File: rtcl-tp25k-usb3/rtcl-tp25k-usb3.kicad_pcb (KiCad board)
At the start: 4 copper layers, 80 x 35 mm, 82 parts, among them J1 ZX360D-B-10P(30), J10 SSQ-106-02-F-D-RA, J2 0525592253, J3 BTB-DF40C-60DS-0.4V(51), J4 DF40C-60DS-0.4V(51), J5 JTAG, Q1 2SK3018, Q2 2SK3018, U1 FT601Q, U2 TPD4E05U06DQA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

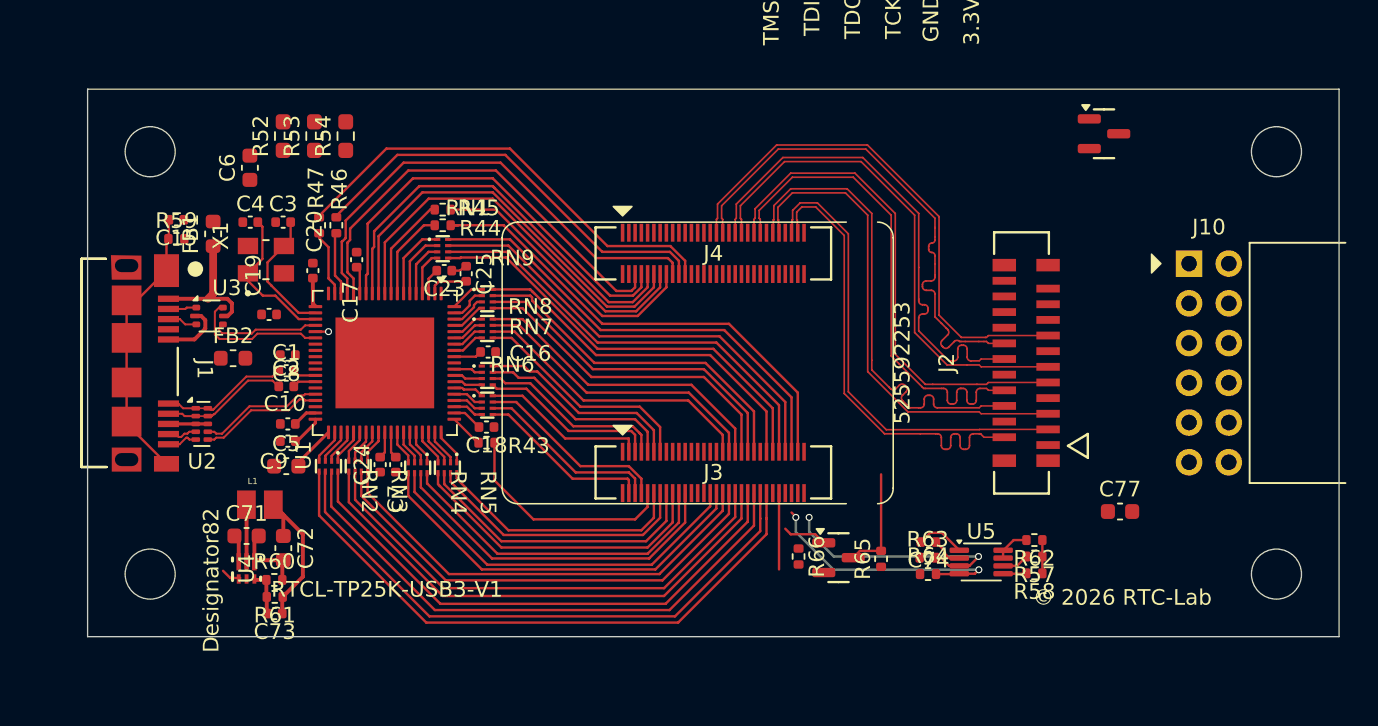
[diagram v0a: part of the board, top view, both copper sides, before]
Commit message: Update KiCad project files and add pin assignment documentation
- Changed selection filter for footprints in the KiCad project rules file to true.
- Adjusted minimum clearance value in the KiCad project settings from 0.5 to 0.2.
- Added new Excel file for pin assignments with lengths to the documentation directory.
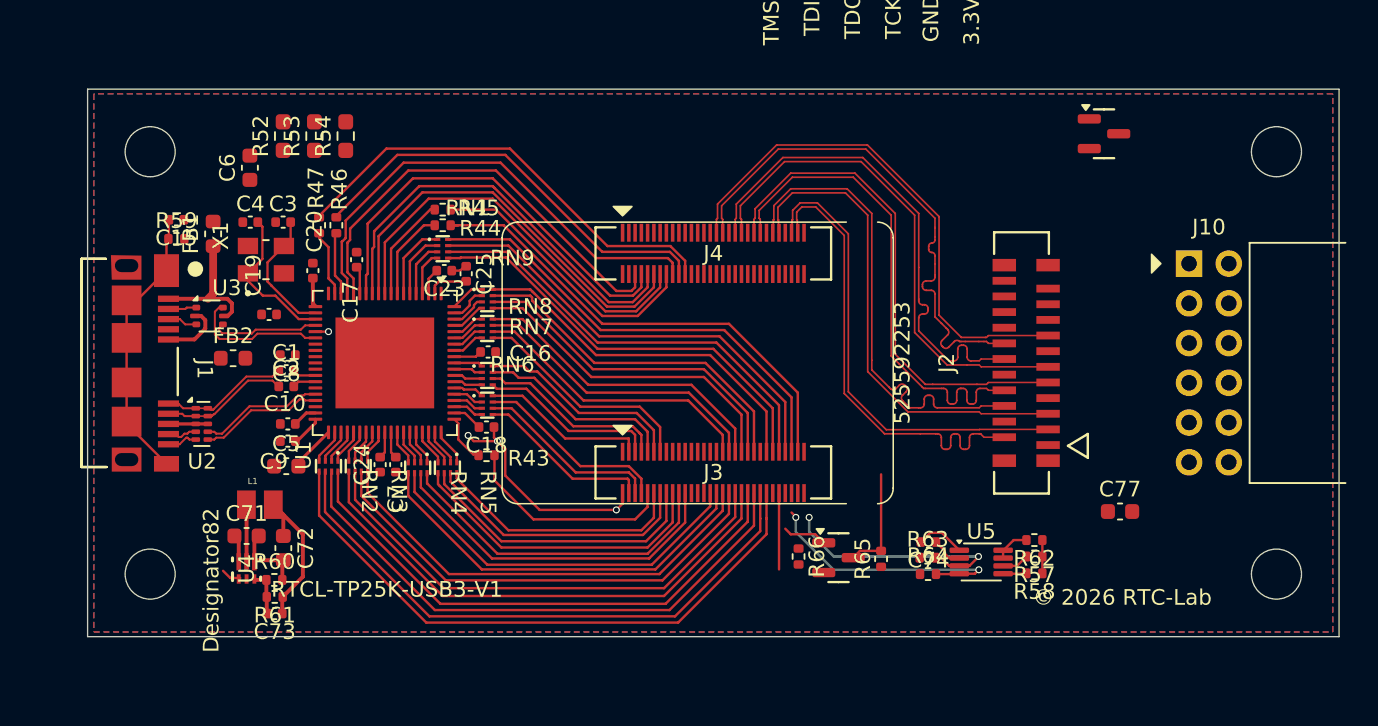
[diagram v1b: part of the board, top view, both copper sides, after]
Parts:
- moved R43 0.80 mm to (135.5, 105.9)
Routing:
- net GND: track 15.6 -> 30.3 mm, vias 0 -> 3
- net /FT601_D23: track 0.00 -> 1.85 mm
- net /FT601_CLK: track 2.17 -> 3.11 mm
- net /K5_IOT63B: track 14.4 -> 13.6 mm
- added copper zone on B.Cu, net GND
- added copper zone on F.Cu, net GND
- added copper zone on In1.Cu, net GND

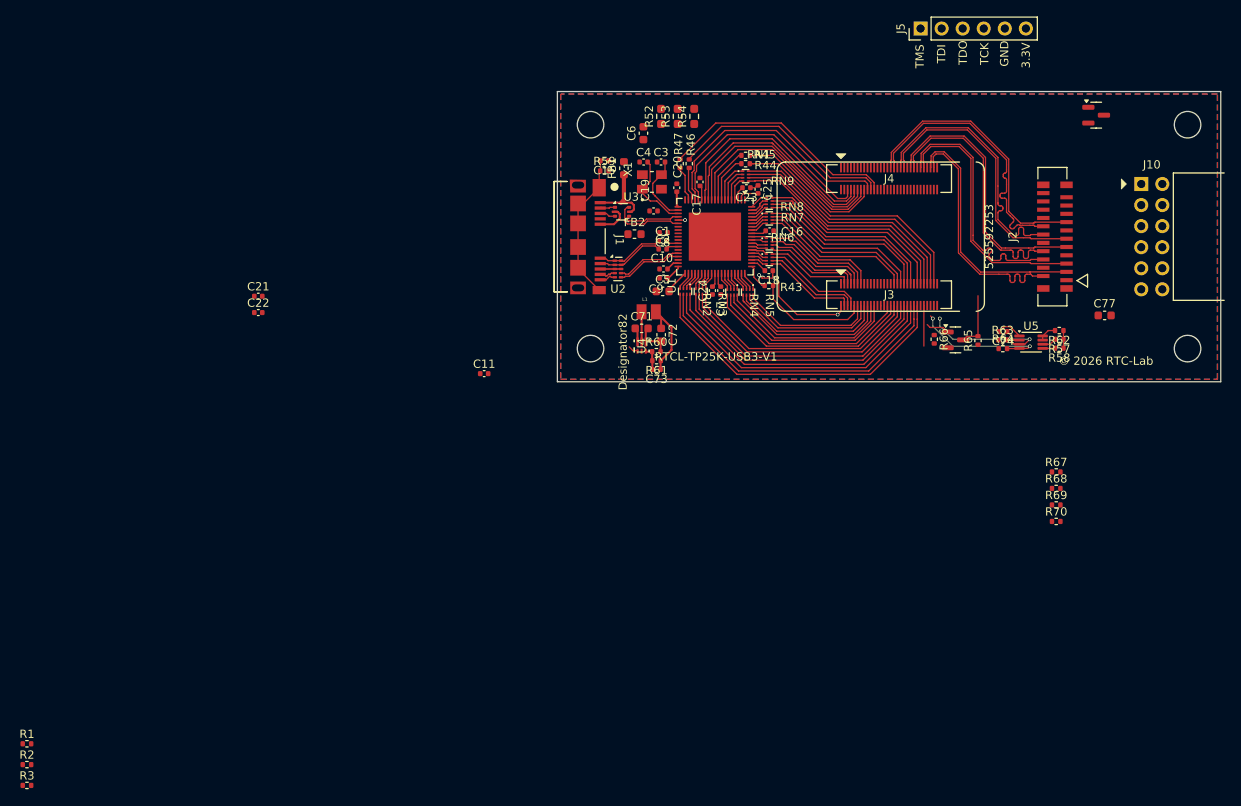
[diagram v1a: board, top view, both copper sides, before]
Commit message: Update KiCad project files and component definitions
- Changed active layer from 4 to 0 in the project settings.
- Enabled text visibility in the board settings.
- Adjusted clearance values for various classes in the project configuration to improve design rules.
- Updated UUIDs for multiple elements in the component definition file to ensure uniqueness and avoid conflicts.
- Removed redundant lines in the component definition for clarity and conciseness.
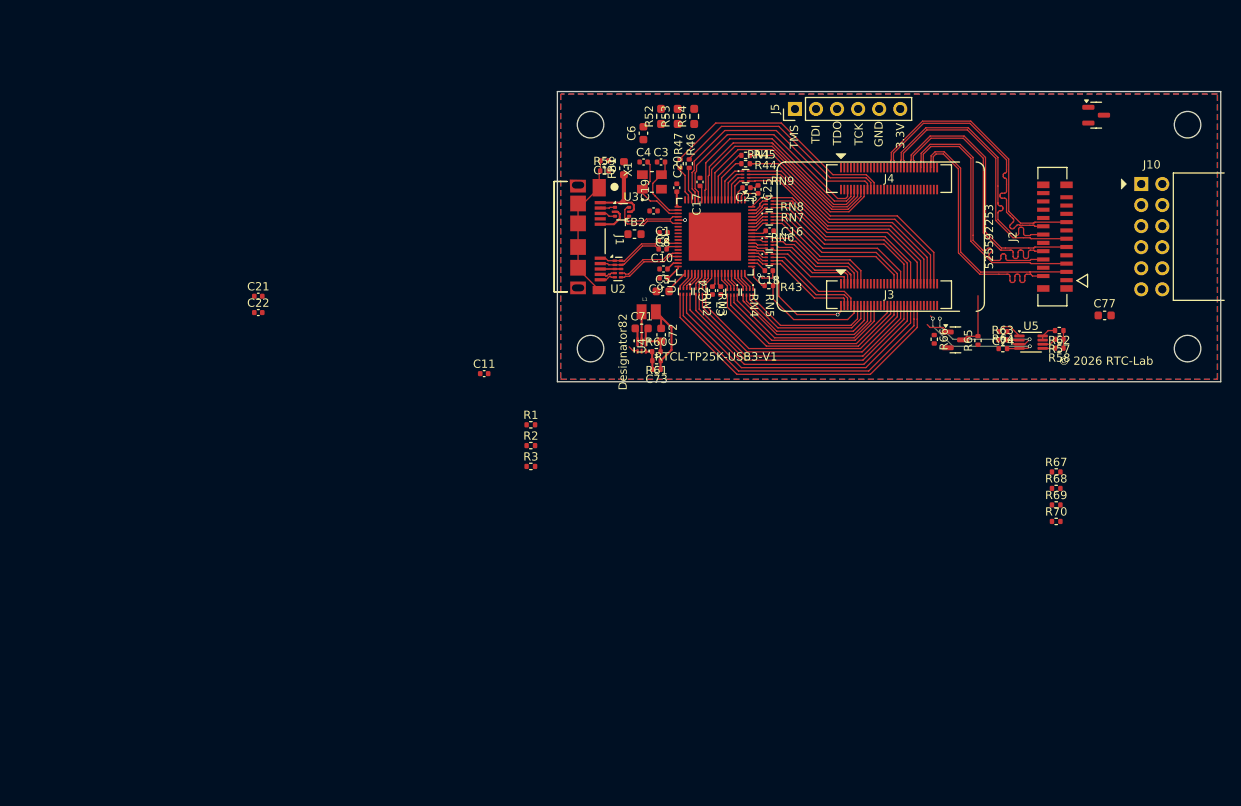
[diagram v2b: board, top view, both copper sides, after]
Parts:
- moved R3 71.9 mm to (106.8, 127.7)
- moved R1 71.9 mm to (106.8, 122.7)
- moved R2 71.9 mm to (106.8, 125.2)
- moved J5 18.0 mm to (138.7, 84.6)
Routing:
- net /E11_IOL3A: track 4.89 -> 0.01 mm
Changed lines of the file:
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@@
 		(capping no)
 		(filling no)
+		(zone_defaults)
 		(pcbplotparams
 			(layerselection 0x00000000_00000000_55555555_5755f5ff)
@@
 	(footprint "Connector_PinHeader_2.54mm:PinHeader_1x06_P2.54mm_Vertical"
 		(layer "F.Cu")
-		(at 153.8 74.9 90)
+		(at 138.65 84.6 90)
 		(descr "Through hole straight pin header, 1x06, 2.54mm pitch, single row")
 		(tags "Through hole pin header THT 1x06 2.54mm single row")
@@
 	(footprint "Resistor_SMD:R_0402_1005Metric"
 		(layer "F.Cu")
-		(at 46.03 161.16)
+		(at 106.8 122.69)
 		(descr "Resistor SMD 0402 (1005 Metric), square (rectangular) end terminal, IPC-7351 nominal, (Body size source: IPC-SM-782 page 72, https://www.pcb-3d.com/wordpress/wp-content/uploads/ipc-sm-782a_amendment_1_and_2.pdf)")
 		(tags "resistor")
@@
 		(sheetname "/")
 		(sheetfile "rtcl-tp25k-usb3.kicad_sch")
-		(units
-			(unit
-				(name "A")
-				(pins "1" "2" "3" "4" "5" "6" "7" "8" "9" "10" "11" "12" "13" "14" "15"
-					"16" "17" "18" "19" "20" "21" "22"
-				)
-			)
-		)
 		(attr smd)
 		(duplicate_pad_numbers_are_jumpers no)
@@
 		)
 		(fp_line
-			(start 9.619983 -3.320001)
-			(end -9.619983 -3.320001)
-			(stroke
-				(width 0.127)
-				(type solid)
-			)
-			(layer "F.CrtYd")
-		)
-		(fp_line
-			(start -9.619983 -3.320001)
-			(end -9.619983 2.72)
-			(stroke
-				(width 0.127)
-				(type solid)
-			)
-			(layer "F.CrtYd")
-		)
-		(fp_line
 			(start -9.619983 -3.320001)
 			(end -9.619983 2.72)
@@
 		)
 		(fp_line
-			(start 9.619983 2.72)
-			(end 9.619983 -3.320001)
-			(stroke
-				(width 0.127)
-				(type solid)
-			)
-			(layer "F.CrtYd")
-		)
-		(fp_line
-			(start -9.619983 2.72)
-			(end 9.619983 2.72)
-			(stroke
-				(width 0.127)
-				(type solid)
-			)
-			(layer "F.CrtYd")
-		)
-		(fp_line
 			(start -9.619983 2.72)
 			(end 9.619983 2.72)
@@
 	(footprint "Resistor_SMD:R_0402_1005Metric"
 		(layer "F.Cu")
-		(at 46.03 163.67)
+		(at 106.8 125.2)
 		(descr "Resistor SMD 0402 (1005 Metric), square (rectangular) end terminal, IPC-7351 nominal, (Body size source: IPC-SM-782 page 72, https://www.pcb-3d.com/wordpress/wp-content/uploads/ipc-sm-782a_amendment_1_and_2.pdf)")
 		(tags "resistor")
@@
 	(footprint "Resistor_SMD:R_0402_1005Metric"
 		(layer "F.Cu")
-		(at 46.03 166.18)
+		(at 106.8 127.71)
 		(descr "Resistor SMD 0402 (1005 Metric), square (rectangular) end terminal, IPC-7351 nominal, (Body size source: IPC-SM-782 page 72, https://www.pcb-3d.com/wordpress/wp-content/uploads/ipc-sm-782a_amendment_1_and_2.pdf)")
 		(tags "resistor")
@@
 	)
 	(gr_text "TMS"
-		(at 154.3 79.7 90)
+		(at 139.15 89.4 90)
 		(layer "F.SilkS")
 		(effects
@@
 	)
 	(gr_text "TDI"
-		(at 156.9 79.1 90)
+		(at 141.75 88.8 90)
 		(layer "F.SilkS")
 		(effects
@@
 	)
 	(gr_text "TDO"
-		(at 159.5 79.3 90)
+		(at 144.35 89 90)
 		(layer "F.SilkS")
 		(effects
@@
 	)
 	(gr_text "TCK"
-		(at 162.1 79.3 90)
+		(at 146.95 89 90)
 		(layer "F.SilkS")
 		(effects
@@
 	)
 	(gr_text "GND"
-		(at 164.5 79.5 90)
+		(at 149.35 89.2 90)
 		(layer "F.SilkS")
 		(effects
@@
 	)
 	(gr_text "3.3V"
-		(at 167.1 79.7 90)
+		(at 151.95 89.4 90)
 		(layer "F.SilkS")
 		(effects
@@
 	)
 	(segment
-		(start 154.199999 108.32)
-		(end 154.199999 113.200001)
-		(width 0.156464)
-		(layer "F.Cu")
-		(net "/E11_IOL3A")
-	)
-	(segment
 		(start 155.399999 105.68)
 		(end 155.399999 101.899999)
@@
 		)
 		(min_thickness 0.25)
-		(fill
+		(fill yes
 			(thermal_gap 0.5)
 			(thermal_bridge_width 0.5)

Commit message: Refactor PCB and schematic files for improved layout and component management
- Updated active layer in the PCB design from 31 to 25 for better visibility.
- Disabled text display in the PCB design to reduce clutter.
- Removed unnecessary junctions and wires from the schematic to streamline the design.
- Adjusted component placements and properties, including resistors and capacitors, for better alignment and readability.
- Changed UUIDs for various elements in the schematic and PCB files to ensure uniqueness and prevent conflicts.
- Updated the connector module with new UUIDs and cleaned up unnecessary geometry.
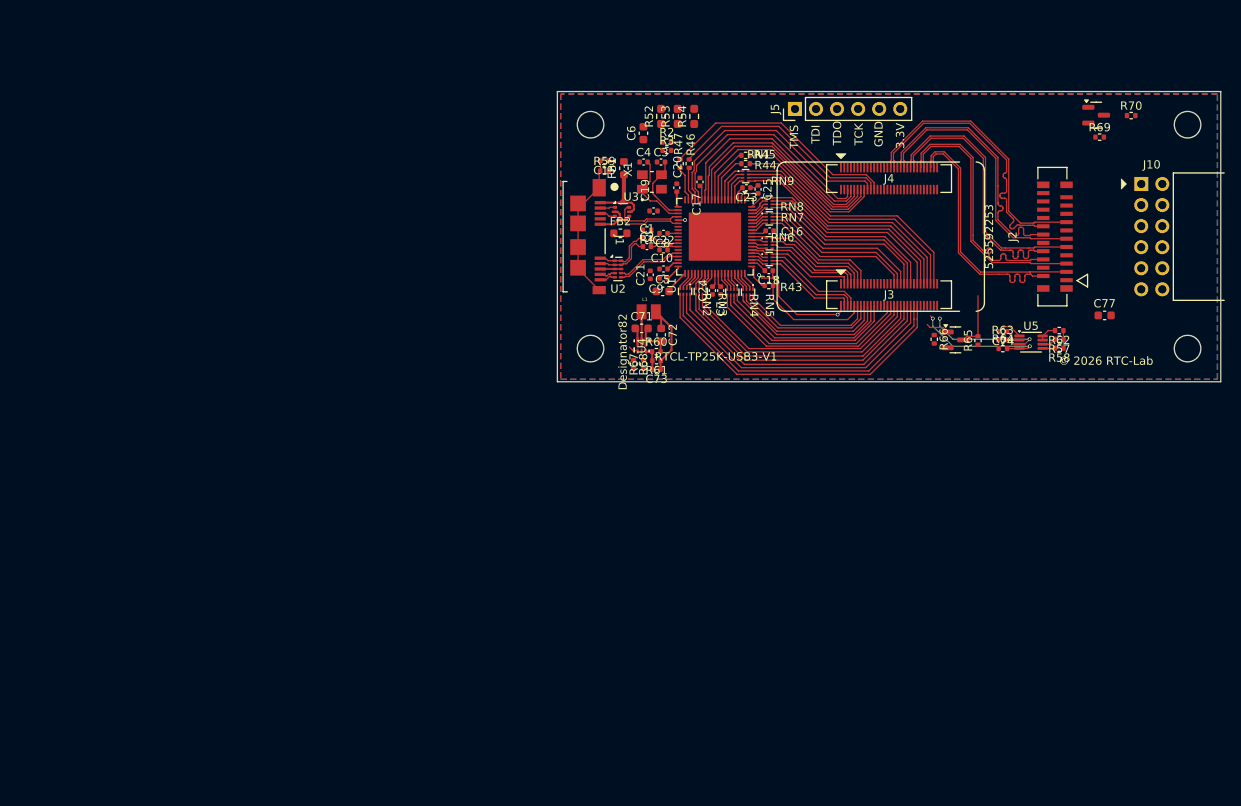
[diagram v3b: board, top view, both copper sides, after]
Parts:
- removed C11: 0.1uF, Capacitor_SMD:C_0402_1005Metric
- R3: value 10k -> 4.7k
- moved R68 53.1 mm to (119.2, 115.4), turned to -90 degrees
- moved R67 51.4 mm to (120.4, 115.4), turned to 90 degrees
- moved R70 49.8 mm to (179.2, 85.4)
- moved C22 49.5 mm to (122.8, 101.6)
- moved C21 47.3 mm to (121.2, 104.6), turned to 90 degrees
- moved R69 44.7 mm to (175.4, 88.0)
- moved R3 41.5 mm to (123.2, 89.6)
- moved R2 40.1 mm to (123.2, 88.6)
- moved R1 27.3 mm to (120.8, 99.2), turned to 180 degrees
- moved C1 1.92 mm to (120.8, 100.2)
- moved C2 1.92 mm to (120.8, 101.2)
- moved FB2 1.70 mm to (117.6, 99.6)
- moved C8 0.10 mm to (122.8, 99.6)
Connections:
- R3 pad 1: /FT601_RESET -> GND
- R3 pad 2: VCC -> /FT601_RESET
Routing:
- net /FT601_TODP: track 1.51 -> 3.59 mm
- net /FT601_TODN: track 1.51 -> 3.59 mm
- net +3V3: track 4.70 -> 5.98 mm
- net /USB_SSTX_P: track 8.40 -> 7.32 mm
- net /USB_SSTX_N: track 8.31 -> 7.50 mm

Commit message: WIP
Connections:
- J4 pad 18: /FT601_WAKEUP -> /G2_IOR24A_40P
- J4 pad 32: /H4_IOB89B_40P -> /FT601_WAKEUP
- R44 pad 2: /B10_IOL12B -> /G2_IOR24A_40P
- R46 pad 2: /G1_IOR24B_40P -> /H1_IOB91A_40P
- R47 pad 2: /L4_IOR31A_40P -> /H2_IOB91B_40P
- RN1 pad 5: /D10_IOL9B -> /J1_IOR33A_40P
- RN1 pad 6: /C11_IOL5A -> /L3_IOR31B_40P
- RN1 pad 7: /C10_IOL5B -> /L4_IOR31A_40P
- RN1 pad 8: /B11_IOL12A -> /G1_IOR24B_40P
- RN9 pad 7: /G10_IOT7B -> /G4_IOB89A_40P
- RN9 pad 8: /D11_IOL9A -> /J2_IOR33B_40P
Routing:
- net /H2_IOB91B_40P: track 0.00 -> 32.2 mm
- net /B10_IOL12B: track 46.5 -> 15.6 mm
- net /H1_IOB91A_40P: track 0.01 -> 30.2 mm
- net /B11_IOL12A: track 46.5 -> 16.9 mm
- net /C10_IOL5B: track 31.7 -> 2.83 mm
- net /C11_IOL5A: track 29.5 -> 1.29 mm
- net /D10_IOL9B: track 27.5 -> 0.00 mm
- net /D11_IOL9A: track 23.3 -> 0.00 mm
- net /G10_IOT7B: track 22.5 -> 0.00 mm
- net /J1_IOR33A_40P: track 0.00 -> 21.3 mm
- net /L3_IOR31B_40P: track 0.00 -> 20.6 mm
- net /G4_IOB89A_40P: track 0.00 -> 19.6 mm
- net /G2_IOR24A_40P: track 0.00 -> 19.2 mm
- net /J2_IOR33B_40P: track 0.00 -> 18.6 mm
- net /L4_IOR31A_40P: track 29.1 -> 20.0 mm
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
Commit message: WIP
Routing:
- net GND: track 30.3 -> 47.9 mm, vias 3 -> 5
- net /L9_IOT31A_40P: track 10.7 -> 12.0 mm
- net /H5_IOT61A: track 11.3 -> 12.3 mm
- net /K9_IOT31B_40P: track 11.5 -> 12.5 mm
- net /J8_IOT56A_40P: track 12.1 -> 13.0 mm
- net /J5_IOT61B: track 11.9 -> 12.8 mm
- net /L11_IOT11B: track 39.2 -> 40.0 mm
- net /L5_IOT63A: track 12.5 -> 13.2 mm
- net /K8_IOT56B_40P: track 12.8 -> 13.4 mm
- net /K11_IOT11A: track 37.9 -> 38.5 mm
- net /K6_IOT23B_USB_N: track 25.7 -> 26.3 mm
- net /K10_IOT15B_40P: track 36.2 -> 36.7 mm
- net /L10_IOT15A_40P: track 34.8 -> 35.4 mm
- net /G5_IOT72B: track 22.5 -> 23.1 mm
- net /L8_IOT19B_40P: track 33.2 -> 33.8 mm
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
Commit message: WIP
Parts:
- added LED1: 150060VS55040, LED_SMD:LED_0603_1608Metric, F.Cu at (179.6, 114.2)
- Q1, Q2: value 2SK3018 -> NTK3134NT1G; footprint PCM_JLCPCB:Q_SOT-23 -> Package_TO_SOT_SMD:SOT-723
- R70: value 330 -> 100
- moved R70 31.0 mm to (179.7, 116.4), turned to 180 degrees
- moved Q2 26.6 mm to (179.6, 111.5), turned to -90 degrees
- moved R66 26.2 mm to (175.2, 95.2), turned to 0 degrees
- moved C74 25.8 mm to (166.1, 85.7)
- moved R58 25.8 mm to (172.9, 87.7)
- moved R62 25.8 mm to (172.9, 85.6)
- moved R63 25.8 mm to (166.1, 86.7)
- moved R57 25.8 mm to (172.9, 86.7)
- moved R64 25.8 mm to (166.1, 87.8)
- moved U5 25.8 mm to (169.5, 87.0)
- moved Q1 23.3 mm to (175.3, 96.8), turned to -90 degrees
- moved R69 22.3 mm to (179.6, 109.9), turned to 180 degrees
- moved R65 20.3 mm to (175.3, 98.4), turned to 0 degrees
- moved J5 12.6 mm to (151.2, 84.4), turned to -90 degrees
- moved C77 4.68 mm to (177.3, 105.0), turned to 90 degrees
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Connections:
- Q1 pad 1: /C10_IOL5B -> /C11_IOL5A
- R63 pad 2: /B10_IOL12B -> /D11_IOL9A
- R64 pad 2: /B11_IOL12A -> /D10_IOL9B
- R66 pad 2: /C10_IOL5B -> /C11_IOL5A
- R68 pad 1: /C11_IOL5A -> /G10_IOT7B
- U4 pad 1: /C11_IOL5A -> /G10_IOT7B
- U5 pad 3: /B10_IOL12B -> /D11_IOL9A
- U5 pad 4: /B11_IOL12A -> /D10_IOL9B
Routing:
- net /G10_IOT7B: track 0.00 -> 41.6 mm, vias 0 -> 2
- net /D11_IOL9A: track 0.00 -> 30.5 mm, vias 0 -> 2
- net /C11_IOL5A: track 1.29 -> 31.2 mm, vias 0 -> 2
- net /D10_IOL9B: track 0.00 -> 26.1 mm, vias 0 -> 2
- net GND: track 47.9 -> 72.9 mm, vias 5 -> 20
- net +5V: track 3.34 -> 23.2 mm, vias 0 -> 8
- net /B11_IOL12A: track 16.9 -> 0.00 mm, vias 2 -> 0
- net /B10_IOL12B: track 15.6 -> 0.00 mm, vias 2 -> 0
- net /MIPI_SCL: track 1.74 -> 11.9 mm
- net /C1_JTAG_TCK: track 0.00 -> 9.20 mm
- net /B1_JTAG_TMS: track 0.00 -> 8.52 mm, vias 0 -> 1
- net /A2_JTAG_TDO: track 0.00 -> 8.47 mm
- net /MIPI_SDA: track 1.50 -> 9.85 mm
- net +3V3: track 5.98 -> 14.0 mm, vias 1 -> 5
- net /A3_JTAG_TDI: track 0.00 -> 7.59 mm
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
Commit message: WIP
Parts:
- moved R46 0.30 mm to (125.6, 91.2)
- moved C19 0.30 mm to (121.6, 97.2)
- moved R47 0.30 mm to (124.5, 91.2)
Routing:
- net GND: track 72.9 -> 80.3 mm, vias 20 -> 28
- net Net-(U1-DV10): track 6.34 -> 9.32 mm, vias 0 -> 3
- net VCC: track 13.0 -> 15.6 mm, vias 2 -> 5
- net Net-(U1-AVDD): track 2.66 -> 4.72 mm, vias 0 -> 2
- net +3V3: track 14.0 -> 15.4 mm, vias 5 -> 8
- net +5V: track 23.2 -> 23.9 mm, vias 8 -> 9

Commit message: WIP
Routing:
- net /E1_IOB12B_40P: track 0.00 -> 3.41 mm, vias 0 -> 1
- net /D8_RECONFIG: track 0.00 -> 3.29 mm, vias 0 -> 1
- net /F1_IOB26B_40P: track 0.00 -> 3.20 mm, vias 0 -> 1
- net /D1_IOB14B_40P: track 0.00 -> 2.98 mm, vias 0 -> 1
- net /A1_IOB24A_40P: track 0.00 -> 2.59 mm, vias 0 -> 1
- net /F2_IOB26A_40P: track 0.00 -> 2.36 mm, vias 0 -> 1
- net /B2_IOB4A_40P: track 0.00 -> 1.55 mm, vias 0 -> 1
- net /C2_IOB4B_40P: track 0.00 -> 1.45 mm, vias 0 -> 1
